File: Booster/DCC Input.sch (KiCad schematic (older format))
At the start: 14 parts, among them P201 CONN_01X02, P202 CONN_01X02, SW201 FORCE_ENABLE, U201 6N136, U202 LM339

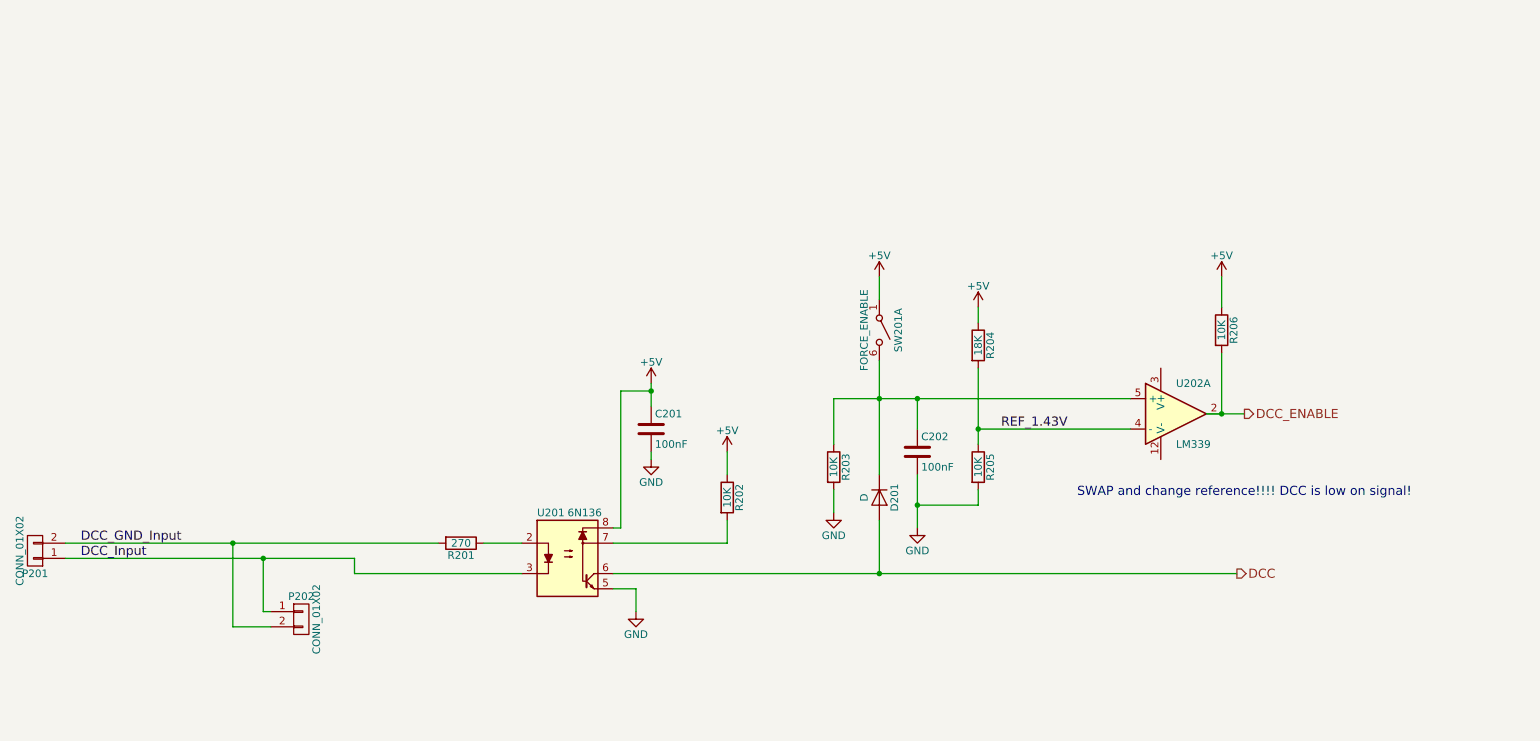
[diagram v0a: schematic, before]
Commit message: Pulse detector circuit included.
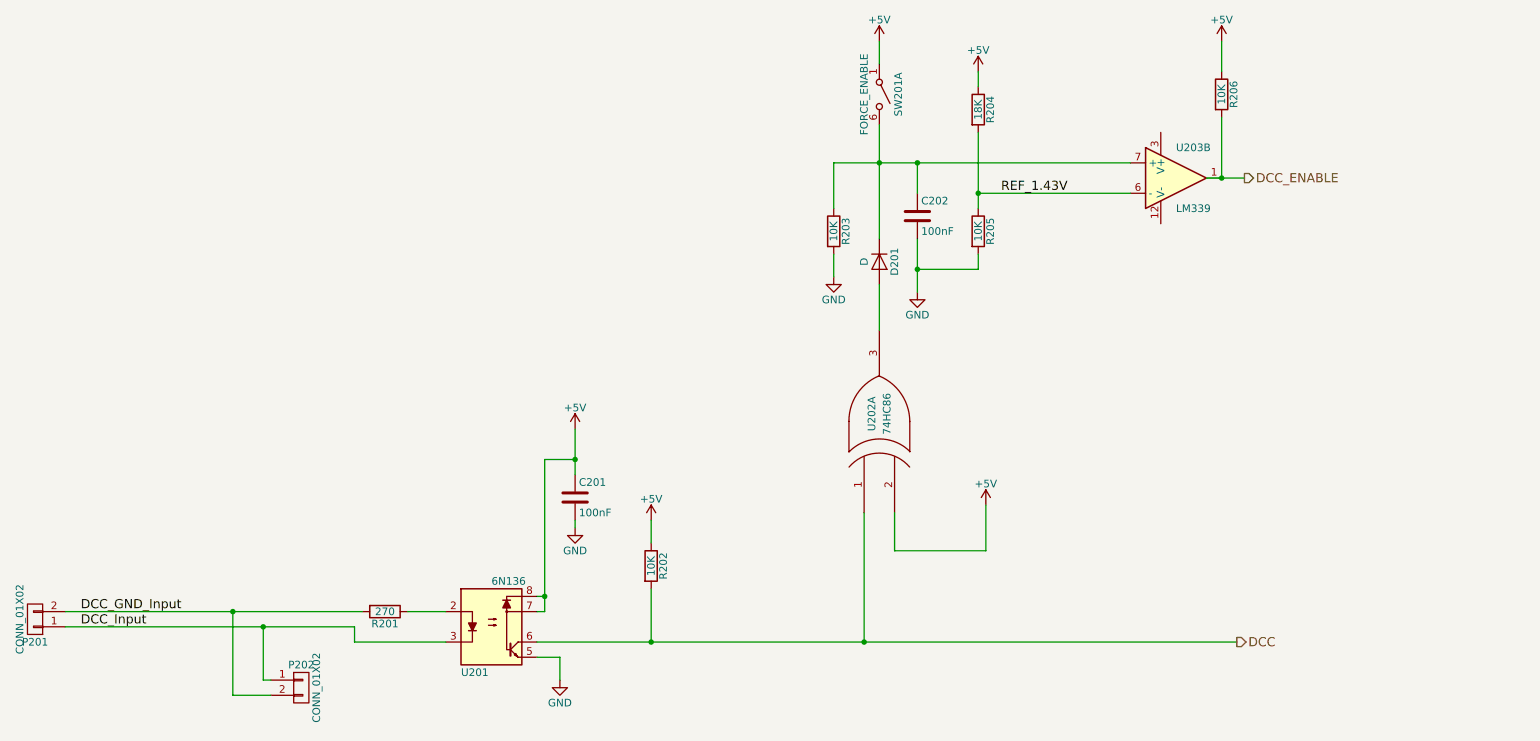
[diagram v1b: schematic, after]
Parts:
- added U202: 74HC86, symbol 74HC86
- renumbered U202 to U203
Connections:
- net +5V: now also U201.7, U202.2 (IN2)
- net DCC: now also R202.2, U202.1 (IN1); no longer D201.2 (A)
- net DCC_ENABLE: now also U203.1; no longer U203.2
- net GND: now also U202.7 (GND)
- net REF_1.43V: now also U203.6 (-); no longer U203.4 (-)
- net at C202.1, D201.1 (K), R203.1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: now also U203.7 (+); no longer U203.5 (+)
- new net: D201.2 (A), U202.3 (OUT)
- new net VCC: U202.14 (VCC)
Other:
- note removed: "SWAP and change reference!!!! DCC is low on signal!"
- moved on the sheet: C201, C202, D201, P201, P202, R201, R202, R203, R204, R205, R206, SW201A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

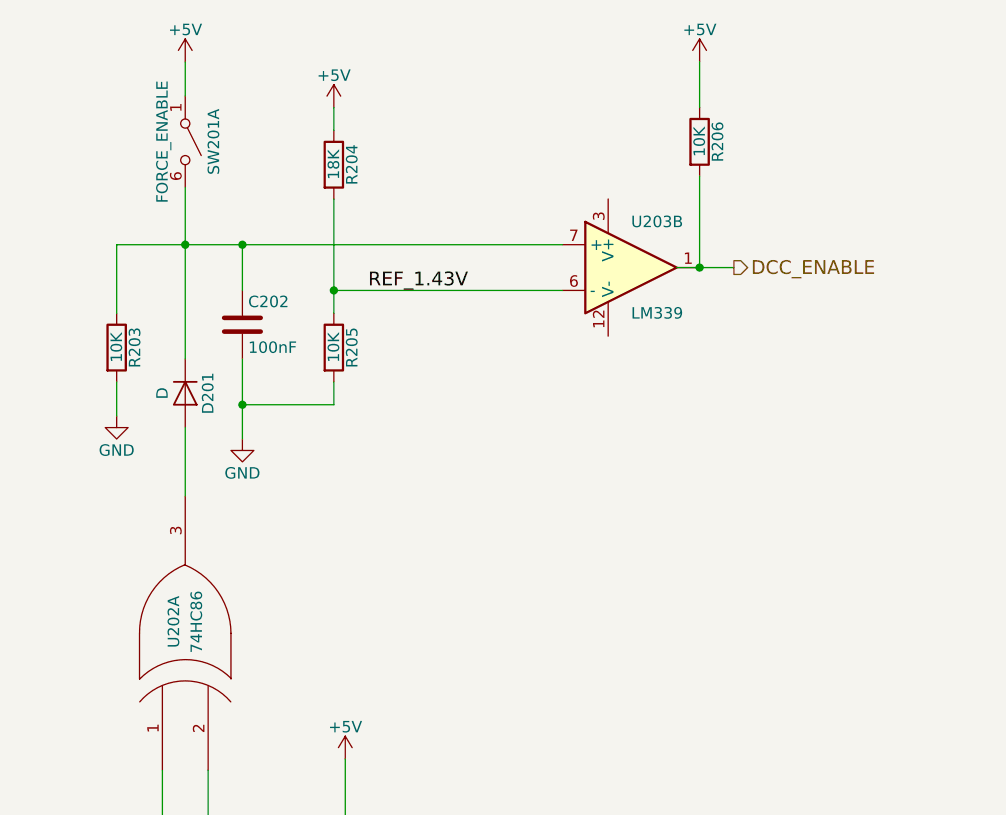
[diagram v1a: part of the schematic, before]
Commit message: Various adjustments based on breadboard prototype.
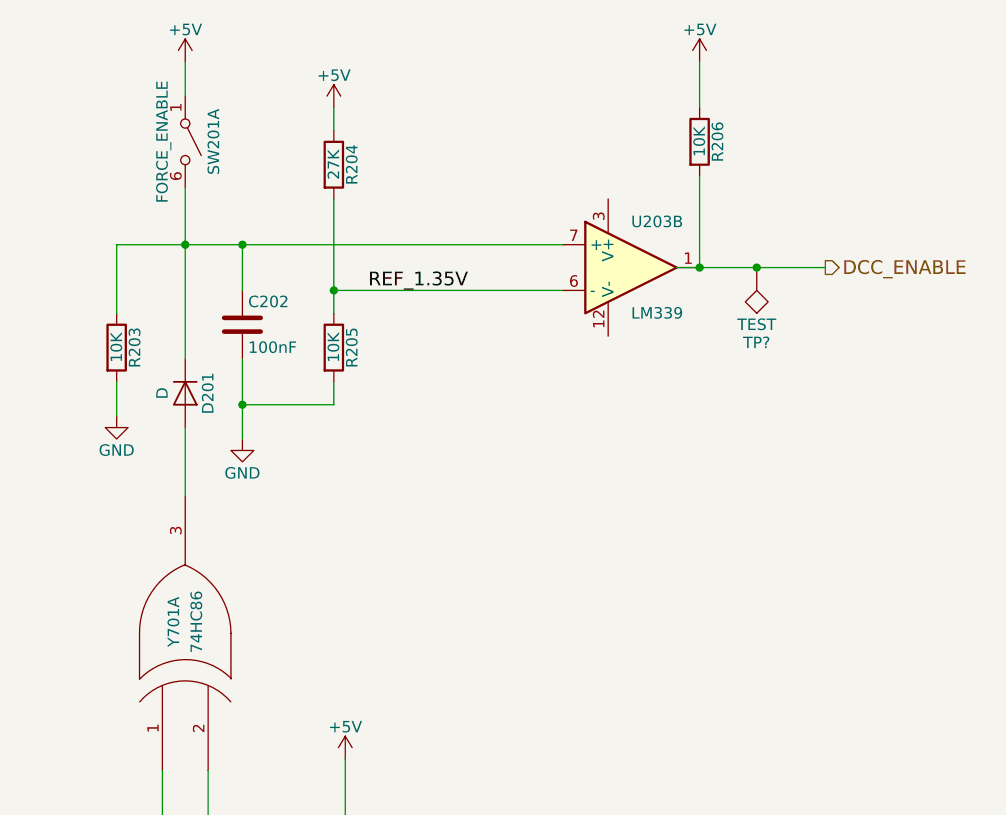
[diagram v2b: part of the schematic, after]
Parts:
- added TP?: TEST, symbol TEST
- R204: value 18K -> 27K
- renumbered U202 to Y701
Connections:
- net DCC_ENABLE: now also TP?.1
- net REF_1.43V renamed REF_1.35V
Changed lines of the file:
@@
 $EndComp
 $Comp
-L GND #PWR201
+L GND #PWR01
 U 1 1 59E8F260
 P 4800 5250
-F 0 "#PWR201" H 4800 5000 50  0001 C CNN
+F 0 "#PWR01" H 4800 5000 50  0001 C CNN
 F 1 "GND" H 4800 5100 50  0000 C CNN
 F 2 "" H 4800 5250 50  0001 C CNN
@@
 Text HLabel 9250 5000 2    60   Output ~ 0
 DCC
-Text HLabel 9300 1950 2    60   Output ~ 0
+Text HLabel 9700 1950 2    60   Output ~ 0
 DCC_ENABLE
 $Comp
-L +5V #PWR204
+L +5V #PWR02
 U 1 1 59E8F78D
 P 5400 4200
-F 0 "#PWR204" H 5400 4050 50  0001 C CNN
+F 0 "#PWR02" H 5400 4050 50  0001 C CNN
 F 1 "+5V" H 5400 4340 50  0000 C CNN
 F 2 "" H 5400 4200 50  0001 C CNN
@@
 $EndComp
 $Comp
-L +5V #PWR208
+L +5V #PWR03
 U 1 1 59E8F877
 P 7550 1250
-F 0 "#PWR208" H 7550 1100 50  0001 C CNN
+F 0 "#PWR03" H 7550 1100 50  0001 C CNN
 F 1 "+5V" H 7550 1390 50  0000 C CNN
 F 2 "" H 7550 1250 50  0001 C CNN
@@
 	7150 2350 7150 2700
 $Comp
-L GND #PWR207
+L GND #PWR04
 U 1 1 5A383AD2
 P 7150 2700
-F 0 "#PWR207" H 7150 2450 50  0001 C CNN
+F 0 "#PWR04" H 7150 2450 50  0001 C CNN
 F 1 "GND" H 7150 2550 50  0000 C CNN
 F 2 "" H 7150 2700 50  0000 C CNN
@@
 P 7550 1500
 F 0 "R204" V 7630 1500 50  0000 C CNN
-F 1 "18K" V 7550 1500 50  0000 C CNN
+F 1 "27K" V 7550 1500 50  0000 C CNN
 F 2 "" V 7480 1500 50  0000 C CNN
 F 3 "" H 7550 1500 50  0000 C CNN
@@
 	6600 2450 6600 2600
 $Comp
-L GND #PWR205
+L GND #PWR05
 U 1 1 5A38E8FE
 P 6600 2600
-F 0 "#PWR205" H 6600 2350 50  0001 C CNN
+F 0 "#PWR05" H 6600 2350 50  0001 C CNN
 F 1 "GND" H 6600 2450 50  0000 C CNN
 F 2 "" H 6600 2600 50  0000 C CNN
@@
 Connection ~ 6900 1850
 Wire Wire Line
-	9050 1950 9300 1950
+	9050 1950 9700 1950
 Wire Wire Line
 	9150 1950 9150 1550
@@
 	9150 1250 9150 1050
 $Comp
-L +5V #PWR210
+L +5V #PWR06
 U 1 1 5A38EB05
 P 9150 1050
-F 0 "#PWR210" H 9150 900 50  0001 C CNN
+F 0 "#PWR06" H 9150 900 50  0001 C CNN
 F 1 "+5V" H 9150 1190 50  0000 C CNN
 F 2 "" H 9150 1050 50  0001 C CNN
@@
 $EndComp
 Text Label 7700 2050 0    60   ~ 0
-REF_1.43V
+REF_1.35V
 $Comp
 L SW_SPST_x03 SW201
@@
 	6900 1200 6900 1050
 $Comp
-L +5V #PWR206
+L +5V #PWR07
 U 1 1 5A38FAC1
 P 6900 1050
-F 0 "#PWR206" H 6900 900 50  0001 C CNN
+F 0 "#PWR07" H 6900 900 50  0001 C CNN
 F 1 "+5V" H 6900 1190 50  0000 C CNN
 F 2 "" H 6900 1050 50  0001 C CNN
@@
 	4650 5000 9250 5000
 $Comp
-L GND #PWR203
+L GND #PWR08
 U 1 1 5A3A1465
 P 4900 4250
-F 0 "#PWR203" H 4900 4000 50  0001 C CNN
+F 0 "#PWR08" H 4900 4000 50  0001 C CNN
 F 1 "GND" H 4900 4100 50  0000 C CNN
 F 2 "" H 4900 4250 50  0001 C CNN
@@
 	4900 3600 4900 3900
 $Comp
-L +5V #PWR202
+L +5V #PWR09
 U 1 1 5A3A1566
 P 4900 3600
-F 0 "#PWR202" H 4900 3450 50  0001 C CNN
+F 0 "#PWR09" H 4900 3450 50  0001 C CNN
 F 1 "+5V" H 4900 3740 50  0000 C CNN
 F 2 "" H 4900 3600 50  0001 C CNN
@@
 	5400 4350 5400 4200
 $Comp
-L 74HC86 U202
+L 74HC86 Y701
 U 1 1 5A3AC211
 P 6900 3550
-F 0 "U202" H 6950 3600 50  0000 C CNN
+F 0 "Y701" H 6950 3600 50  0000 C CNN
 F 1 "74HC86" H 6950 3500 50  0000 C CNN
 F 2 "" H 6900 3550 50  0000 C CNN
@@
 	7600 4400 7600 4100
 $Comp
-L +5V #PWR209
+L +5V #PWR010
 U 1 1 5A3ACB63
 P 7600 4100
-F 0 "#PWR209" H 7600 3950 50  0001 C CNN
+F 0 "#PWR010" H 7600 3950 50  0001 C CNN
 F 1 "+5V" H 7600 4240 50  0000 C CNN
 F 2 "" H 7600 4100 50  0001 C CNN
@@
 	4700 4800 4650 4800
 Connection ~ 4700 4700
+$Comp
+L TEST TP?
+U 1 1 5A3E0919
+P 9400 1950
+F 0 "TP?" H 9400 2250 50  0000 C BNN
+F 1 "TEST" H 9400 2200 50  0000 C CNN
+F 2 "" H 9400 1950 50  0000 C CNN
+F 3 "" H 9400 1950 50  0000 C CNN
+	1    9400 1950
+	-1   0    0    1
+$EndComp
+Connection ~ 9400 1950
 $EndSCHEMATC

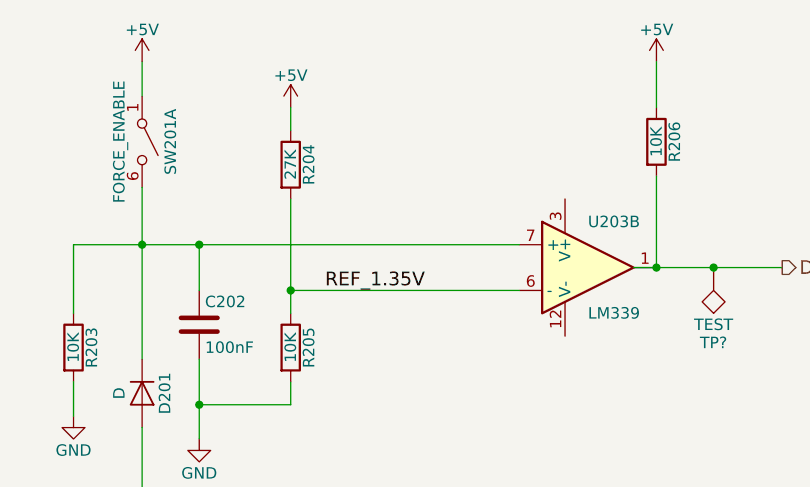
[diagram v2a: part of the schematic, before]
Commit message: Replaced NAND gate with AND as the additional NOT gates ended up only used to negate the NAND gates directly. One extra AND gate used to allow resetting overcurrent by either master switch or DCC disable/enable.
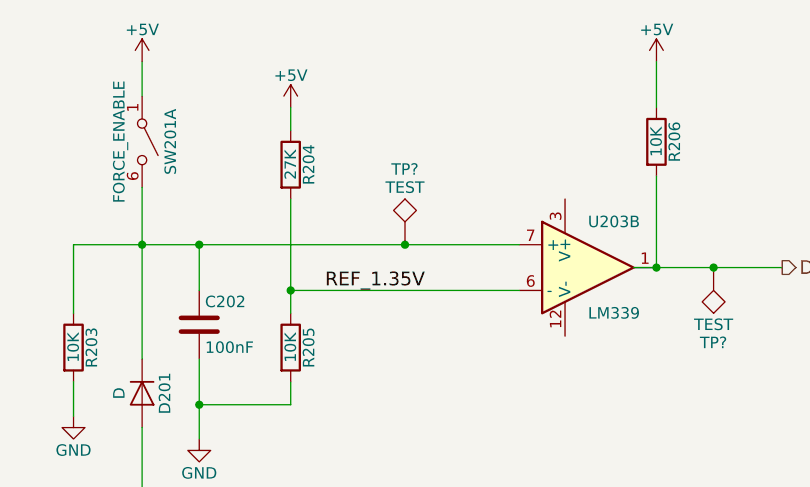
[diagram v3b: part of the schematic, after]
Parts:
- added TP?: TEST, symbol TEST
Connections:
- net at C202.1, D201.1 (K), R203.1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: now also TP?.1
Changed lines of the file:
@@
 	0    1    1    0
 $EndComp
-Wire Wire Line
-	1550 4800 3500 4800
 $Comp
 L C C201
@@
 	1    0    0    -1
 $EndComp
-Wire Wire Line
-	1550 4900 3450 4900
 Text Label 1650 4800 0    60   ~ 0
 DCC_GND_Input
@@
 	1    0    0    -1
 $EndComp
-Wire Wire Line
-	2900 5250 2850 5250
-Wire Wire Line
-	2850 5250 2850 4900
-Connection ~ 2850 4900
-Wire Wire Line
-	2650 4800 2650 5350
-Wire Wire Line
-	2650 5350 2900 5350
-Connection ~ 2650 4800
 $Comp
 L D D201
@@
 	0    1    1    0
 $EndComp
-Wire Wire Line
-	6900 1600 6900 2350
 $Comp
 L C C202
@@
 	1    0    0    -1
 $EndComp
-Wire Wire Line
-	6600 1850 8550 1850
-Wire Wire Line
-	7150 2350 7150 2700
 $Comp
 L GND #PWR04
@@
 	1    0    0    -1
 $EndComp
-Connection ~ 7150 1850
-Connection ~ 6800 5000
-Wire Wire Line
-	3450 4900 3450 5000
 $Comp
 L LM339 U203
@@
 	1    0    0    -1
 $EndComp
-Wire Wire Line
-	7550 2450 7550 2550
-Wire Wire Line
-	7550 2550 7150 2550
-Connection ~ 7150 2550
-Wire Wire Line
-	7550 1350 7550 1250
-Wire Wire Line
-	7150 1850 7150 2050
-Wire Wire Line
-	7550 1650 7550 2150
-Wire Wire Line
-	7550 2050 8550 2050
-Connection ~ 7550 2050
 $Comp
 L R R203
@@
 	1    0    0    -1
 $EndComp
-Wire Wire Line
-	6600 2450 6600 2600
 $Comp
 L GND #PWR05
@@
 	1    0    0    -1
 $EndComp
-Wire Wire Line
-	6600 2150 6600 1850
-Connection ~ 6900 1850
-Wire Wire Line
-	9050 1950 9700 1950
-Wire Wire Line
-	9150 1950 9150 1550
-Connection ~ 9150 1950
 $Comp
 L R R206
@@
 	1    0    0    -1
 $EndComp
-Wire Wire Line
-	9150 1250 9150 1050
 $Comp
 L +5V #PWR06
@@
 	0    1    1    0
 $EndComp
-Wire Wire Line
-	6900 1200 6900 1050
 $Comp
 L +5V #PWR07
@@
 	-1   0    0    1
 $EndComp
-Wire Wire Line
-	4650 5100 4800 5100
-Wire Wire Line
-	4650 5000 9250 5000
 $Comp
 L GND #PWR08
@@
 	1    0    0    -1
 $EndComp
-Wire Wire Line
-	4900 4250 4900 4200
-Wire Wire Line
-	4700 3800 4900 3800
-Wire Wire Line
-	4900 3600 4900 3900
 $Comp
 L +5V #PWR09
@@
 	1    0    0    -1
 $EndComp
-Connection ~ 4900 3800
-Wire Wire Line
-	4650 4700 4700 4700
-Wire Wire Line
-	4700 3800 4700 4800
-Wire Wire Line
-	4800 5100 4800 5250
-Wire Wire Line
-	5400 4650 5400 5000
-Wire Wire Line
-	5400 4350 5400 4200
 $Comp
 L 74HC86 Y701
@@
 	0    -1   -1   0
 $EndComp
-Wire Wire Line
-	3450 5000 4050 5000
-Wire Wire Line
-	3800 4800 4050 4800
-Wire Wire Line
-	6800 4150 6800 5000
-Wire Wire Line
-	6900 2950 6900 2650
-Wire Wire Line
-	7000 4150 7000 4400
-Wire Wire Line
-	7000 4400 7600 4400
-Wire Wire Line
-	7600 4400 7600 4100
 $Comp
 L +5V #PWR010
@@
 	1    0    0    -1
 $EndComp
-Connection ~ 5400 5000
-Wire Wire Line
-	4700 4800 4650 4800
-Connection ~ 4700 4700
 $Comp
 L TEST TP?
@@
 	-1   0    0    1
 $EndComp
+$Comp
+L TEST TP?
+U 1 1 5A3F7C3F
+P 8050 1850
+F 0 "TP?" H 8050 2150 50  0000 C BNN
+F 1 "TEST" H 8050 2100 50  0000 C CNN
+F 2 "" H 8050 1850 50  0000 C CNN
+F 3 "" H 8050 1850 50  0000 C CNN
+	1    8050 1850
+	1    0    0    -1
+$EndComp
+Wire Wire Line
+	6600 1850 8550 1850
+Connection ~ 8050 1850
 Connection ~ 9400 1950
+Connection ~ 4700 4700
+Wire Wire Line
+	4700 4800 4650 4800
+Connection ~ 5400 5000
+Wire Wire Line
+	7600 4400 7600 4100
+Wire Wire Line
+	7000 4400 7600 4400
+Wire Wire Line
+	7000 4150 7000 4400
+Wire Wire Line
+	6900 2950 6900 2650
+Wire Wire Line
+	6800 4150 6800 5000
+Wire Wire Line
+	3800 4800 4050 4800
+Wire Wire Line
+	3450 5000 4050 5000
+Wire Wire Line
+	5400 4350 5400 4200
+Wire Wire Line
+	5400 4650 5400 5000
+Wire Wire Line
+	4800 5100 4800 5250
+Wire Wire Line
+	4700 3800 4700 4800
+Wire Wire Line
+	4650 4700 4700 4700
+Connection ~ 4900 3800
+Wire Wire Line
+	4900 3600 4900 3900
+Wire Wire Line
+	4700 3800 4900 3800
+Wire Wire Line
+	4900 4250 4900 4200
+Wire Wire Line
+	4650 5000 9250 5000
+Wire Wire Line
+	4650 5100 4800 5100
+Wire Wire Line
+	6900 1200 6900 1050
+Wire Wire Line
+	9150 1250 9150 1050
+Connection ~ 9150 1950
+Wire Wire Line
+	9150 1950 9150 1550
+Wire Wire Line
+	9050 1950 9700 1950
+Connection ~ 6900 1850
+Wire Wire Line
+	6600 2150 6600 1850
+Wire Wire Line
+	6600 2450 6600 2600
+Connection ~ 7550 2050
+Wire Wire Line
+	7550 2050 8550 2050
+Wire Wire Line
+	7550 1650 7550 2150
+Wire Wire Line
+	7150 1850 7150 2050
+Wire Wire Line
+	7550 1350 7550 1250
+Connection ~ 7150 2550
+Wire Wire Line
+	7550 2550 7150 2550
+Wire Wire Line
+	7550 2450 7550 2550
+Wire Wire Line
+	3450 4900 3450 5000
+Connection ~ 6800 5000
+Connection ~ 7150 1850
+Wire Wire Line
+	7150 2350 7150 2700
+Wire Wire Line
+	6900 1600 6900 2350
+Connection ~ 2650 4800
+Wire Wire Line
+	2650 5350 2900 5350
+Wire Wire Line
+	2650 4800 2650 5350
+Connection ~ 2850 4900
+Wire Wire Line
+	2850 5250 2850 4900
+Wire Wire Line
+	2900 5250 2850 5250
+Wire Wire Line
+	1550 4900 3450 4900
+Wire Wire Line
+	1550 4800 3500 4800
 $EndSCHEMATC

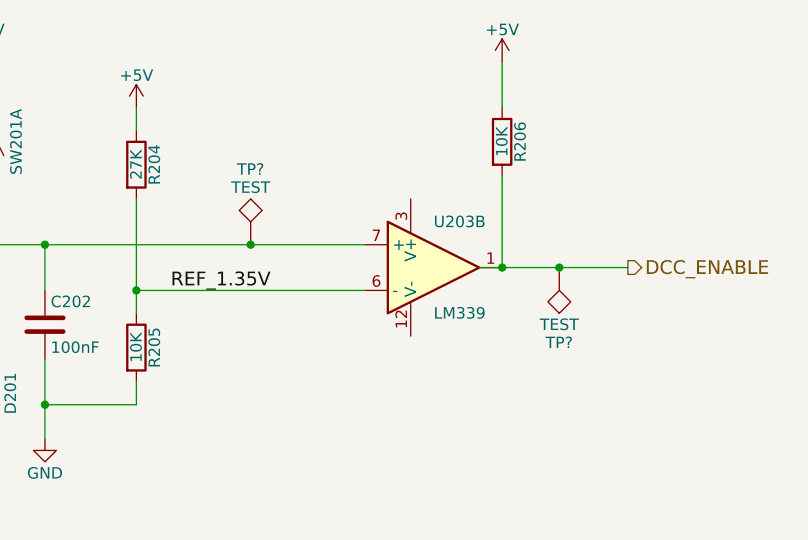
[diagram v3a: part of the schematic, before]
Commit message: Annotation, fix missing connection.
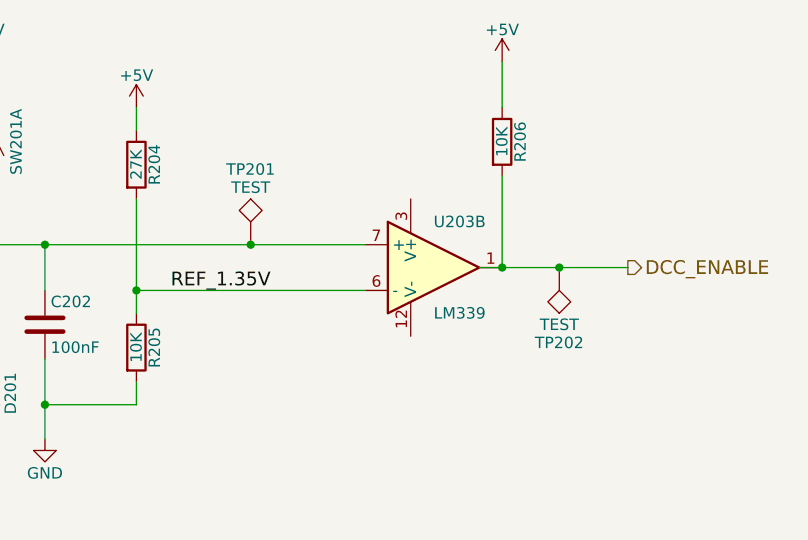
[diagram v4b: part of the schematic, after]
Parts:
- gave numbers to parts that had none: 2
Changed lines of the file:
@@
 $EndComp
 $Comp
-L TEST TP?
+L TEST TP202
 U 1 1 5A3E0919
 P 9400 1950
-F 0 "TP?" H 9400 2250 50  0000 C BNN
+F 0 "TP202" H 9400 2250 50  0000 C BNN
 F 1 "TEST" H 9400 2200 50  0000 C CNN
 F 2 "" H 9400 1950 50  0000 C CNN
@@
 $EndComp
 $Comp
-L TEST TP?
+L TEST TP201
 U 1 1 5A3F7C3F
 P 8050 1850
-F 0 "TP?" H 8050 2150 50  0000 C BNN
+F 0 "TP201" H 8050 2150 50  0000 C BNN
 F 1 "TEST" H 8050 2100 50  0000 C CNN
 F 2 "" H 8050 1850 50  0000 C CNN
